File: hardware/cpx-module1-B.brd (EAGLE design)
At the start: 85.1 x 128.5 mm, 6 parts, among them T1 TOUCHPADROUND1, T2 TOUCHPADROUND1, T3 TOUCHPADROUND1, T4 TOUCHPADROUND1, U1 CIRCUITPLAYGROUNDEXPRESS

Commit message: fixed broken stuff
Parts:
- removed T1, T2, T3, T4: TOUCHPADROUND1, todstuff:TOUCHPAD1
- added C1, C2, C3, C4: 3pF, rcl:C0603
- added C5: 10uF, rcl:C0603
- added C6: 100nF, rcl:C0603
- added D1: 1N4004, adafruit:DO41-10
- added IC2: MCP6004, gm-ics:SO14
- added IC3: LM4040DIM3-5.0, texas:DBZ_R-PDSO-G3
- added J1, J2, J3, J4, J5, J6, J7, J8: WQP-PJ301M-12_JACK, thonkiconn:WQP-PJ301M-12_JACK
- added R1, R11, R13, R15, R3, R5, R7, R9: 33k, adafruit:R0603
- added R10, R14, R2, R6: 100k, adafruit:R0603
- added R12, R16, R4, R8: 50k, adafruit:R0603
- added R18: 10k, adafruit:R0603
- added U$1: POWER, eurorack:POWER_16
- added VR1, VR2, VR3, VR4: 10k, SparkFun-Resistors:POT-PTH-ALPS-KIT
- moved J10 89.8 mm to (-21.7, 81.2)
- moved U1 4.00 mm to (0.00, 0.00)
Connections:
- new net +12V: U$1.10, U$1.9
- new net +3V3: U1.3V3L, VR1.P$1, VR2.P$1, VR3.P$1, VR4.P$1
- new net +5V: D1.A, U$1.11, U$1.12
- new net -12V: C5.2, R18.2, U$1.1, U$1.2
- new net A0ALT: J8.P$2
- new net A1ALT: J7.P$2
- new net A2ALT: J6.P$2
- new net A3ALT: J5.P$2
- new net A4_JACK: J1.P$2, R2.1
- new net A4_KNOB: VR1.P$2
- new net A5_JACK: J2.P$2, R6.1
- new net A5_KNOB: VR2.P$2
- new net A6_JACK: J3.P$2, R10.1
- new net A6_KNOB: VR3.P$2
- new net A7_JACK: J4.P$2, R14.1
- new net A7_KNOB: VR4.P$2
- new net N$2: C2.1, IC2.6, R5.1, R6.2, R7.2, R8.2
- new net N$3: C3.1, IC2.9, R10.2, R11.2, R12.2, R9.1
- new net N$4: C4.1, IC2.13, R13.1, R14.2, R15.2, R16.2
- new net N$5: C1.1, IC2.2, R1.1, R2.2, R3.2, R4.2
- new net REF_-5V: C6.1, IC3.2, R12.1, R16.1, R18.1, R4.1, R8.1
- new net V+: IC2.4
- new net V-: IC2.11
- net A0: now also J8.P$1
- net A1: now also J7.P$1
- net A2: now also J6.P$1; no longer T4.TOUCH
- net A3: now also J5.P$1; no longer T1.TOUCH
- net A4: now also C1.2, IC2.1, R1.2; no longer T3.TOUCH
- net A5: now also C2.2, IC2.7, R5.2; no longer T2.TOUCH
- net A6: now also C3.2, IC2.8, R9.2
- net A7: now also C4.2, IC2.14, R13.2
- net GND: now also C5.1, C6.2, IC2.10, IC2.3, IC2.5, IC3.1, J1.P$3, J2.P$3, J3.P$3, J4.P$3, J5.P$3, J6.P$3, J7.P$3, J8.P$3, U$1.3, U$1.4, U$1.5, U$1.6, U$1.7, U$1.8, VR1.P$3, VR2.P$3, VR3.P$3, VR4.P$3
- net VCC: now also D1.C
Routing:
- net A3: track 69.9 -> 0.00 mm
- net A4: track 69.9 -> 0.00 mm
- net A2: track 62.6 -> 0.00 mm
- net A5: track 62.3 -> 0.00 mm
- net VCC: track 16.4 -> 0.00 mm
- net A0: track 16.4 -> 0.00 mm
- net A7: track 16.2 -> 0.00 mm
- net A1: track 12.0 -> 0.00 mm
- net A6: track 11.8 -> 0.00 mm
- removed copper zone on layer 16, net GND
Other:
- board size 85.1 x 128.5 mm -> 84.7 x 121.9 mm
- board text removed: "A0"
- board text removed: "A1"
- board text removed: "A2"
- board text removed: "A3"
- board text removed: "A4"
- board text removed: "A5"
- board text removed: "A6"
- board text removed: "A7"

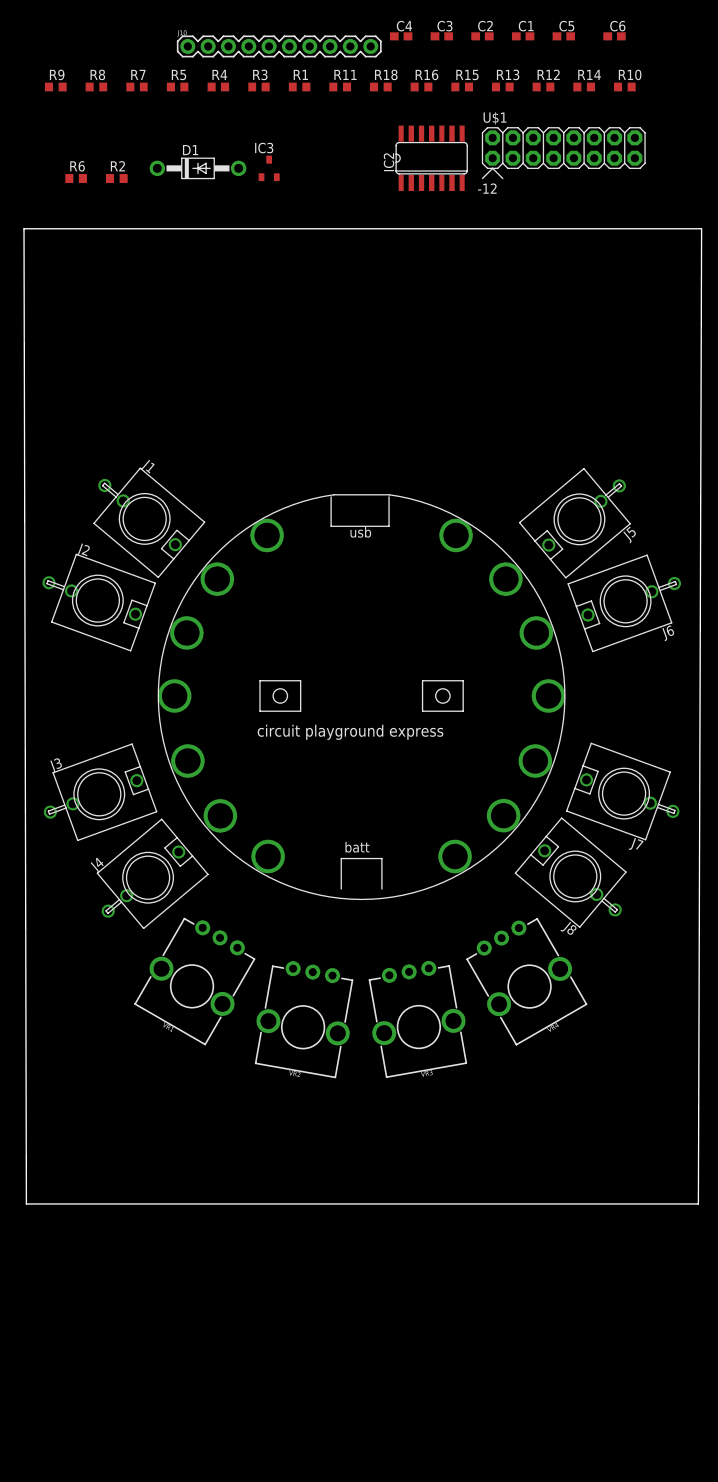
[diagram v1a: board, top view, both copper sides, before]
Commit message: first cut at component placement
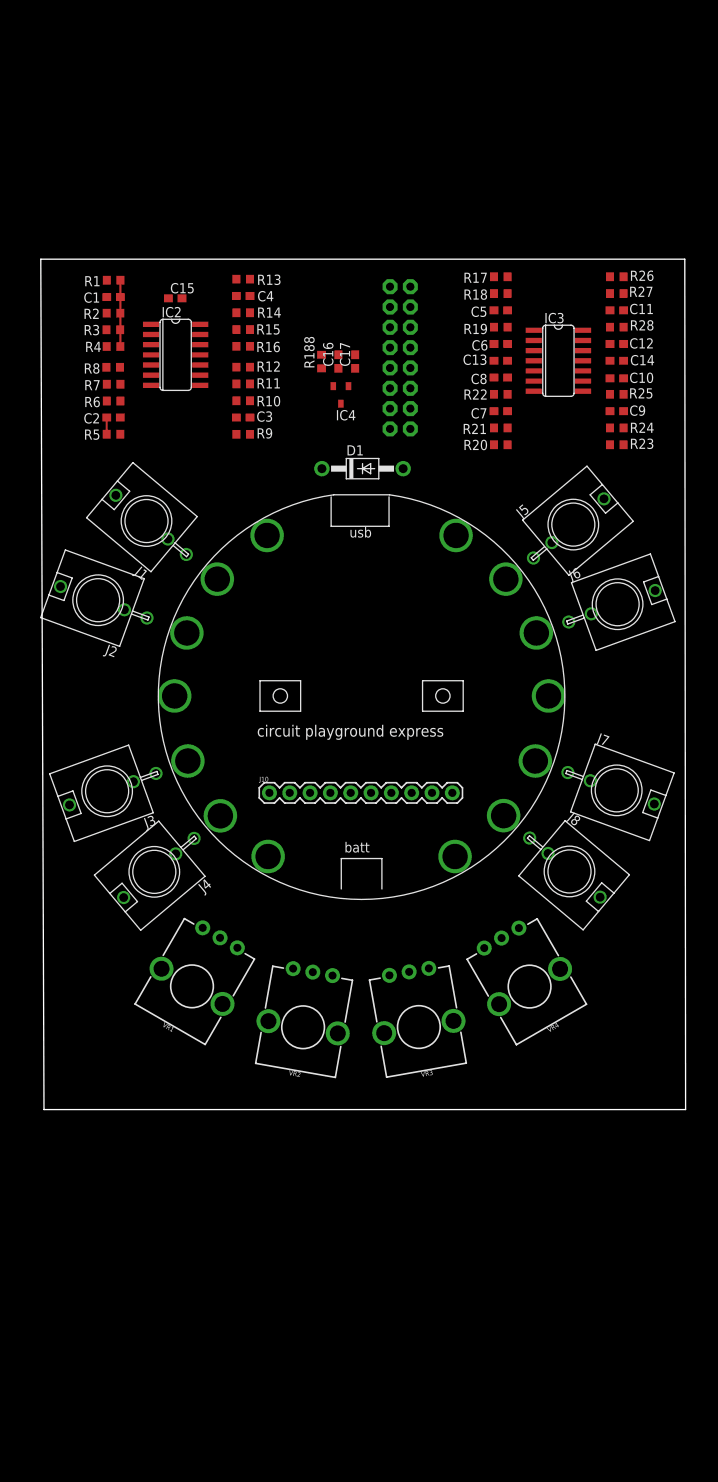
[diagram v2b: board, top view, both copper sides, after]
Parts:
- added C10, C12, C8: 1uF, rcl:C0603
- added C11, C7, C9: 3pF, rcl:C0603
- added C13, C14, C15, C16: 100nF, rcl:C0603
- added C17: 10uF, rcl:C0603
- added IC4: LM4040DIM3-5.0, texas:DBZ_R-PDSO-G3
- added R17, R20, R23, R26: 1k, adafruit:R0603
- added R188, R19, R22, R25, R28: 10k, adafruit:R0603
- added R21, R24, R27: 30k, adafruit:R0603
- C5: value 10uF -> 3pF
- C6: value 100nF -> nonpop
- IC3: value LM4040DIM3-5.0 -> TL074; device texas:DBZ_R-PDSO-G3 -> gm-ics:SO14
- R18: value 10k -> 30k
- moved J10 93.9 mm to (-11.5, -12.1)
- moved C2 66.3 mm to (-31.0, 34.8), turned to 180 degrees
- moved R10 61.7 mm to (-14.8, 36.9), turned to 180 degrees
- moved C1 60.7 mm to (-31.0, 49.9), turned to 180 degrees
- moved C3 53.7 mm to (-14.8, 34.8)
- moved R12 51.3 mm to (-14.8, 41.1), turned to 180 degrees
- moved R14 51.1 mm to (-14.8, 47.9), turned to 180 degrees
- moved R9 49.3 mm to (-14.8, 32.7)
- moved R5 44.1 mm to (-31.0, 32.7), turned to 180 degrees
- moved IC3 43.4 mm to (24.6, 41.9), turned to 270 degrees
- moved D1 42.8 mm to (0.12, 28.4)
- moved C6 41.0 mm to (17.4, 44.0), turned to 180 degrees
- moved R15 40.8 mm to (-14.8, 45.8), turned to 180 degrees
- moved R13 40.4 mm to (-14.8, 52.1)
- moved IC2 40.4 mm to (-23.2, 42.6), turned to 270 degrees
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- renumbered U1 to IC1
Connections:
- removed net A0ALT: J8.P$2
- removed net A1ALT: J7.P$2
- removed net A2ALT: J6.P$2
- removed net A3ALT: J5.P$2
- removed net V+: IC2.4
- removed net V-: IC2.11
- new net N$1: C5.2, IC3.1, R17.1, R18.2
- new net N$10: C9.2, IC3.8, R23.1, R24.2
- new net N$11: J7.P$1, R20.2
- new net N$12: C9.1, IC3.9, R24.1, R25.2
- new net N$13: J6.P$1, R23.2
- new net N$14: C11.2, IC3.14, R26.1, R27.2
- new net N$15: C11.1, IC3.13, R27.1, R28.2
- new net N$16: J5.P$1, R26.2
- new net N$6: J8.P$1, R17.2
- new net N$7: C5.1, IC3.2, R18.1, R19.2
- new net N$8: C7.2, IC3.7, R20.1, R21.2
- new net N$9: C7.1, IC3.6, R21.1, R22.2
- net +12V: now also C13.1, IC3.4
- net +3V3: now also C15.1, IC2.4
- net -12V: now also C14.2, C17.2, IC3.11, R188.2; no longer C5.2, R18.2
- net A0: now also C6.1, R19.1; no longer J8.P$1
- net A1: now also C8.1, R22.1; no longer J7.P$1
- net A2: now also C10.1, R25.1; no longer J6.P$1
- net A3: now also C12.1, R28.1; no longer J5.P$1
- net A4_JACK: now also J1.P$1; no longer J1.P$2
- net A5_JACK: now also J2.P$1; no longer J2.P$2
- net A6_JACK: now also J3.P$1; no longer J3.P$2
- net A7_JACK: now also J4.P$1; no longer J4.P$2
- net GND: now also C10.2, C12.2, C13.2, C14.1, C15.2, C16.2, C17.1, C8.2, IC2.11, IC2.12, IC3.10, IC3.12, IC3.3, IC3.5, IC4.1; no longer C5.1, IC3.1
- net REF_-5V: now also C16.1, IC4.2, R188.1; no longer C6.1, IC3.2, R18.1
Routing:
- net N$5: track 0.00 -> 8.29 mm
- net A5: track 0.00 -> 2.09 mm
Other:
- board size 84.7 x 121.9 mm -> 80.6 x 106.3 mm

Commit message: autorouted as a test
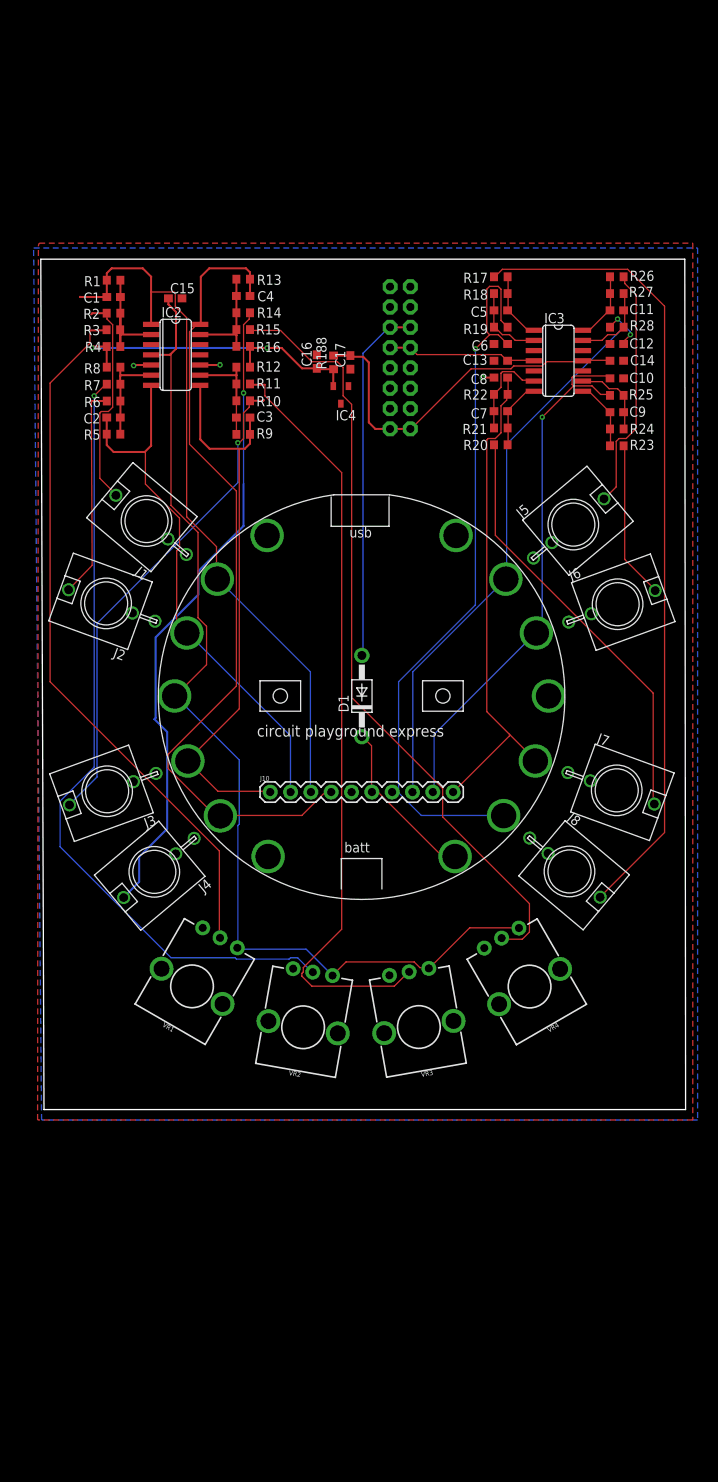
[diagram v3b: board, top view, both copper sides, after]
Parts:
- moved D1 28.4 mm to (0.03, -0.01), turned to 90 degrees
- moved C16 2.70 mm to (-5.60, 41.8)
- moved R188 1.50 mm to (-3.50, 41.7)
- moved J2 1.08 mm to (-31.9, 11.6)
- moved C17 0.61 mm to (-1.40, 41.7)
- moved J10 0.14 mm to (-11.4, -12.0)
- moved C9 0.13 mm to (31.9, 35.5)
- moved R24 0.13 mm to (31.9, 33.4)
- moved R25 0.13 mm to (31.9, 37.6)
- moved R23 0.13 mm to (31.9, 31.3)
- moved R8 0.05 mm to (-31.0, 41.1)
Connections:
- net A4_KNOB: now also R3.1
- net A5_KNOB: now also R7.1
- net A6_KNOB: now also R11.1
- net A7_KNOB: now also R15.1
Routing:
- net +3V3: track 0.00 -> 131.2 mm
- net A7: track 0.00 -> 102.0 mm
- net N$6: track 0.00 -> 100.8 mm
- net A5_KNOB: track 0.00 -> 98.5 mm, vias 0 -> 1
- net A7_KNOB: track 0.00 -> 97.8 mm
- net A6_KNOB: track 0.00 -> 96.6 mm
- net A0: track 0.00 -> 93.6 mm, vias 0 -> 1
- net A4: track 0.00 -> 91.0 mm
- net A4_KNOB: track 0.00 -> 88.9 mm
- net A7_JACK: track 0.00 -> 81.1 mm, vias 0 -> 1
- net A3: track 0.00 -> 74.8 mm, vias 0 -> 2
- net A6: track 0.00 -> 70.6 mm
- net A2: track 0.00 -> 69.3 mm, vias 0 -> 1
- net A5: track 2.09 -> 67.6 mm
- net A1: track 0.00 -> 62.3 mm
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- added copper zone on layer 1, net GND
- added copper zone on layer 16, net GND

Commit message: better routing: hand-routed around opamp, autoroute to connectors
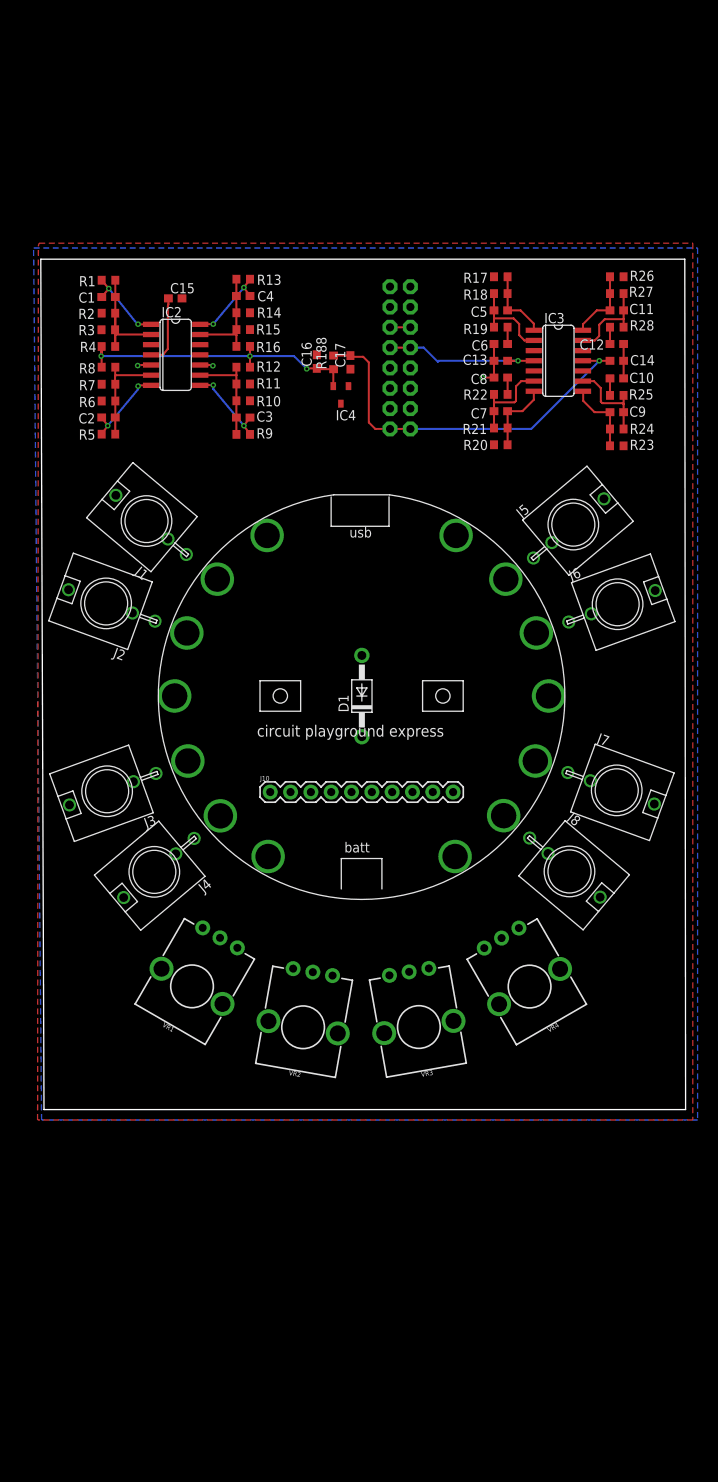
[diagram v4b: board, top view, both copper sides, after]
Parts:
- moved C1 0.64 mm to (-31.6, 49.9)
- moved R1 0.64 mm to (-31.6, 52.0)
- moved R6 0.64 mm to (-31.6, 36.9)
- moved R7 0.64 mm to (-31.6, 39.0)
- moved R8 0.64 mm to (-31.6, 41.1)
- moved C2 0.63 mm to (-31.6, 34.8)
- moved R2 0.63 mm to (-31.6, 47.9)
- moved R3 0.63 mm to (-31.7, 45.8)
- moved R4 0.63 mm to (-31.6, 43.7)
- moved R5 0.63 mm to (-31.6, 32.7)
- turned C12 to 0 degrees
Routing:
- net +3V3: track 131.2 -> 8.77 mm
- net N$6: track 100.8 -> 0.00 mm
- net A5_KNOB: track 98.5 -> 0.00 mm, vias 1 -> 0
- net A7_KNOB: track 97.8 -> 0.00 mm
- net A6_KNOB: track 96.6 -> 0.14 mm
- net A0: track 93.6 -> 2.10 mm, vias 1 -> 0
- net A7: track 102.0 -> 10.5 mm, vias 0 -> 2
- net A4_KNOB: track 88.9 -> 0.11 mm
- net A7_JACK: track 81.1 -> 0.00 mm, vias 1 -> 0
- net A4: track 91.0 -> 10.2 mm, vias 0 -> 2
- net A3: track 74.8 -> 2.10 mm, vias 2 -> 0
- net A2: track 69.3 -> 2.13 mm, vias 1 -> 0
- net A6_JACK: track 61.7 -> 0.00 mm, vias 1 -> 0
- net A1: track 62.3 -> 2.10 mm
- net A6: track 70.6 -> 10.7 mm, vias 0 -> 2
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
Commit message: added protection diodes and filter caps, added pdfs
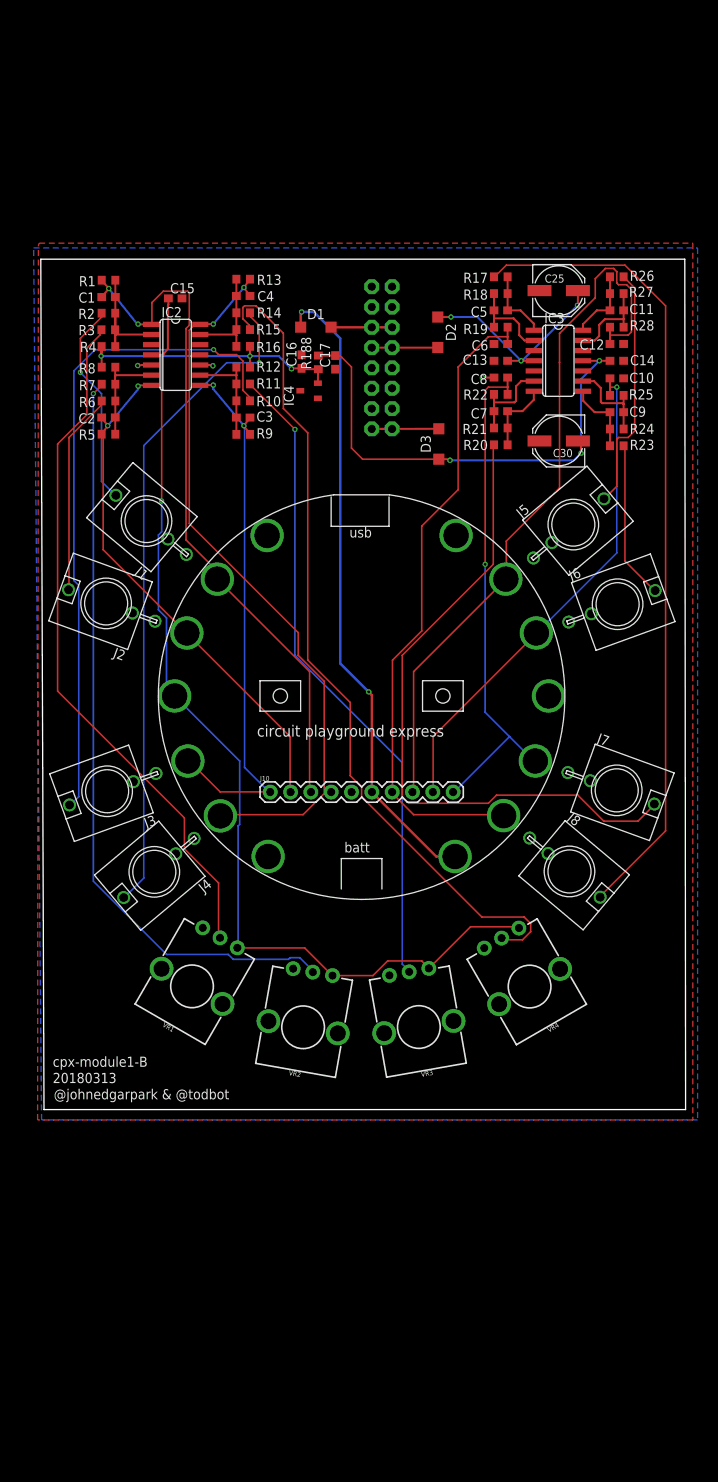
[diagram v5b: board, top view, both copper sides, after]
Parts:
- added C25, C30: 47u, rcl:PANASONIC_D
- added D2, D3: 1N5819HW, diode:SOD123
- D1: value 1N4004 -> 1N5819HW; device adafruit:DO41-10 -> diode:SOD123
- moved D1 46.5 mm to (-5.71, 46.1), turned to 0 degrees
- moved IC4 4.00 mm to (-6.56, 38.2), turned to 90 degrees
- moved U$1 2.29 mm to (2.54, 39.7)
- moved C16 1.91 mm to (-7.50, 41.8)
- moved C17 1.91 mm to (-3.31, 41.7)
- moved R188 1.91 mm to (-5.41, 41.7)
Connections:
- net +5V renamed N$19
- new net N$17: D2.A, U$1.10, U$1.9
- new net N$18: D3.A, U$1.1, U$1.2
- net +12V: now also C25.+, D2.C; no longer U$1.10, U$1.9
- net -12V: now also C30.-, D3.C; no longer U$1.1, U$1.2
- net GND: now also C25.-, C30.+
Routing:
- net +3V3: track 8.77 -> 127.4 mm, vias 0 -> 1
- net A7_KNOB: track 0.00 -> 104.5 mm
- net N$6: track 0.00 -> 101.4 mm
- net A5_KNOB: track 0.00 -> 95.0 mm, vias 0 -> 1
- net A3: track 2.10 -> 90.9 mm
- net A4_KNOB: track 0.11 -> 86.9 mm
- net N$11: track 0.00 -> 83.3 mm
- net A6_JACK: track 0.00 -> 83.2 mm, vias 0 -> 1
- net A7_JACK: track 0.00 -> 83.0 mm, vias 0 -> 1
- net A7: track 10.5 -> 93.1 mm
- net A6_KNOB: track 0.14 -> 81.8 mm, vias 0 -> 1
- net VCC: track 0.00 -> 80.3 mm, vias 0 -> 2
- net A0: track 2.10 -> 81.7 mm
- net A4: track 10.2 -> 87.4 mm
- net A1: track 2.10 -> 64.1 mm, vias 0 -> 1
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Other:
- board text added: "20180313"
- board text added: "@johnedgarpark & @todbot"
- board text added: "cpx-module1-B"

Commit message: added resistors on A1,A2,A3 to potentially allow touch input to work, re-routed lower half a bit better
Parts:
- added R29, R30, R31: 10k, adafruit:R0603
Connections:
- net N$11 renamed A1OUT
- net N$13 renamed A2OUT
- net N$16 renamed A3OUT
- net N$6 renamed A0OUT
- new net N$20: C12.1, R28.1, R29.2
- new net N$21: C10.1, R25.1, R30.2
- new net N$22: C8.1, R22.1, R31.2
- net A1: now also R31.1; no longer C8.1, R22.1
- net A2: now also R30.1; no longer C10.1, R25.1
- net A3: now also R29.1; no longer C12.1, R28.1
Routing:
- net +3V3: track 127.4 -> 146.6 mm
- net A3: track 90.9 -> 76.1 mm, vias 0 -> 1
- net A7_KNOB: track 104.5 -> 116.8 mm
- net A4_KNOB: track 86.9 -> 97.0 mm
- net N$22: track 0.00 -> 7.03 mm
- net N$21: track 0.00 -> 6.68 mm
- net N$20: track 0.00 -> 6.58 mm
- net A4: track 87.4 -> 90.6 mm
- net VCC: track 80.3 -> 83.3 mm
- net -12V: track 63.6 -> 66.5 mm
- net A0OUT: track 101.4 -> 103.7 mm
- net A7: track 93.1 -> 95.4 mm
- net A3OUT: track 30.6 -> 32.1 mm, vias 0 -> 1
- net A2: track 63.1 -> 64.6 mm
- net A5_KNOB: track 95.0 -> 96.3 mm
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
